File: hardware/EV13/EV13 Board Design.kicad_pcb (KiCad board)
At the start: 4 copper layers, 85 x 99.3 mm, 157 parts, among them CN2 Conn_05x02_Female, CN4 Conn_01x06_Female, J1 Conn_01x02_Socket, J10 Conn_01x08_Socket, J2 Conn_02x05_Counter_Clockwise, J3 Conn_02x05_Counter_Clockwise, J4 AudioJack2, J5 AudioJack3, J6 Conn_02x05_Counter_Clockwise, J7 Conn_02x05_Counter_Clockwise, J9 USB_C_Receptacle, SW1 SW_Push, SW3 SW_Push, SW4 SW_Push, SW5 SW_Push, SW6 SW_SPDT, U1 STM32F405RGTx, U11 ESP32-S3-WROOM-1, U13 BM14B(0.8)-24DS-0.4V(53), U2 BQ21040DBV, U3 CH340C, U4 USBLC6-2P6, U5 M24C02-RMN6TP, U6 WM8960CGEFL/RV, U7 TPS63060, U8 STM32F072CBTx, Y1 Crystal_GND24

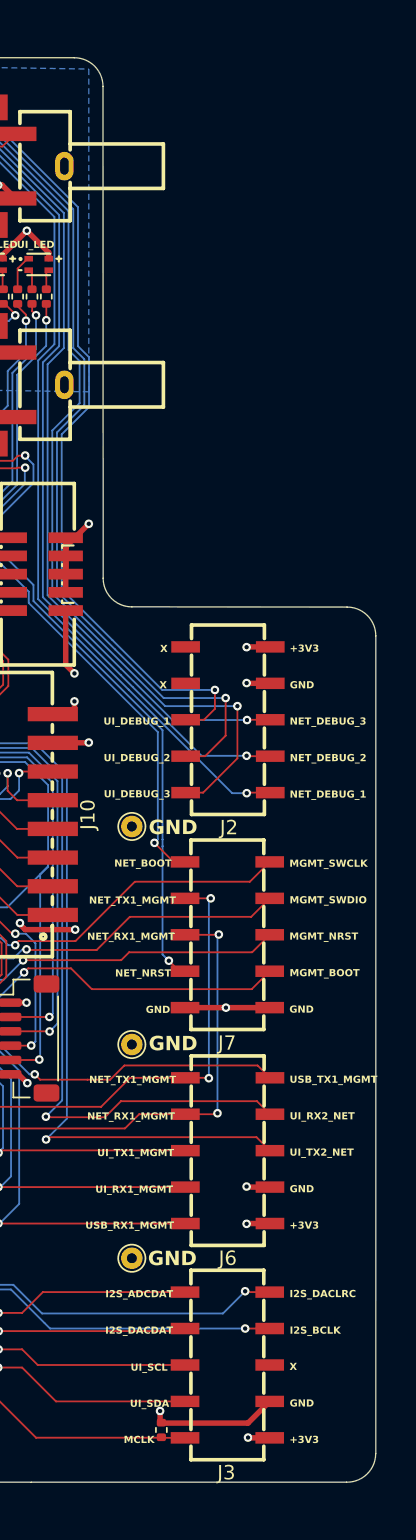
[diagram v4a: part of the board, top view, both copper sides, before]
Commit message: Added 3V3 and GND rails
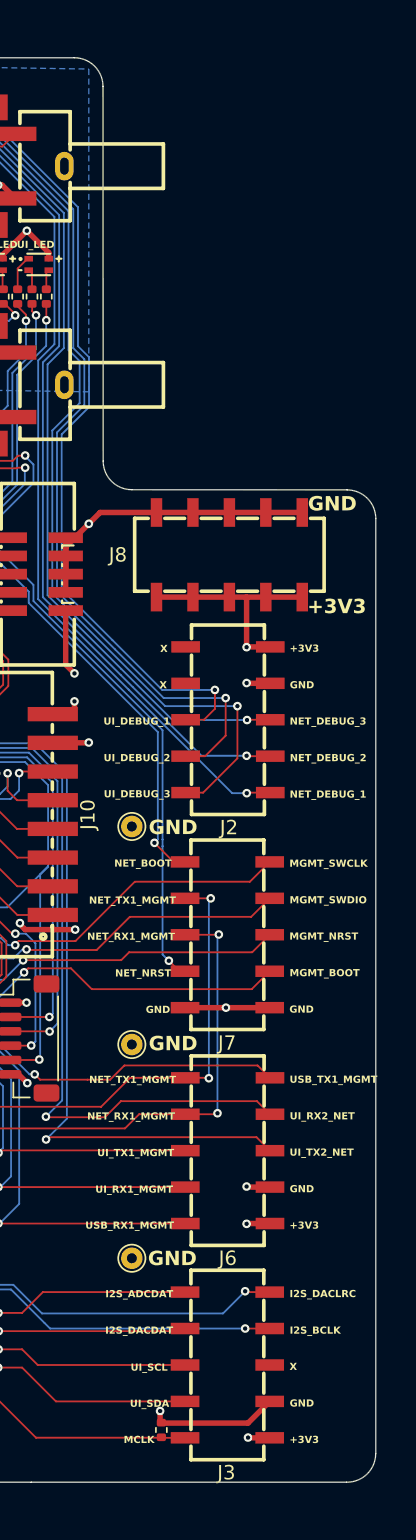
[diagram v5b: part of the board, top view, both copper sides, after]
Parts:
- added J8: Conn_02x05_Counter_Clockwise, Hactar_Footprints:HDR-SMD_10P-P2.54, F.Cu at (188.8, 80.7)
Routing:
- net GND: track 683.9 -> 699.1 mm
- net +3.3V: track 528.3 -> 542.0 mm
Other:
- outline, holes or cut-outs redrawn
